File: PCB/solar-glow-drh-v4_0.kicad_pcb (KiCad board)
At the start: 2 copper layers, 50.8 x 88.9 mm, 67 parts, among them J1 UPDI hdr, SW2 LED master, U1 AVR64DD28 (VQFN28), U3 ADXL367, U5 NT3H2211, U6 TPS22918, U8 AEM10300, U9 TPS7A0233 (SOT23-5*)

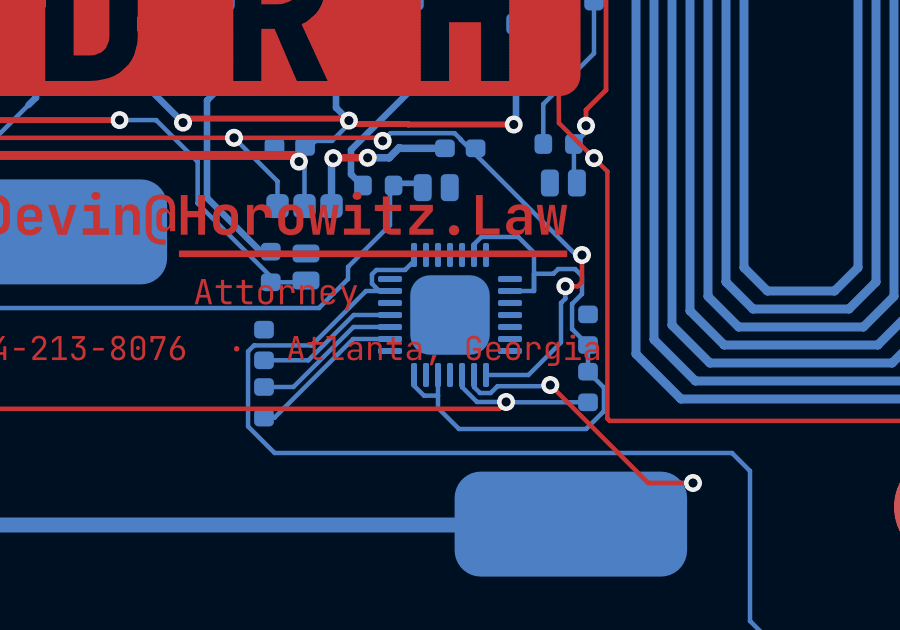
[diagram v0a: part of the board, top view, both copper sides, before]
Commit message: PCB: fix U8 AEM10300 EP land to datasheet; relabel stay-0402 parts
U8 (AEM10300, QFN-28 4x4): the reused AVR land carried a 2.65 mm exposed
pad; e-peas Fig 18 recommends a 2.30 mm thermal land. Shrink U8's EP to
2.30 mm (scoped to U8 only; U1 keeps its 2.65 mm EP). Pad centres are
unchanged so routing is intact, and the smaller EP increases pad-to-EP
clearance. Perimeter pads stay 0.20 mm wide (0.25 mm would drop the
pitch gap to 0.15 mm, below a safe margin over the 0.126 mm floor).

Relabel the three parts that stay 0402 (the package markers were
aspirational TODOs): C26 10uF, C27 10uF (100uF is not an 0402 part and
the 1F supercaps already meet the AEM STO >=100uF minimum), FB1 ferrite.
Values updated in both the board and schematic to stay consistent.

C25 (22uF) and L2 (10uH) are left as-is; they take real 0603 lands in
the follow-up KiCad pass where they can be re-placed and re-routed.

Co-Authored-By: Claude Opus 4.8 <noreply@anthropic.com>
Claude-Session: https://claude.ai/code/session_01PBK3zFENdvoGtn8yP7qPA8
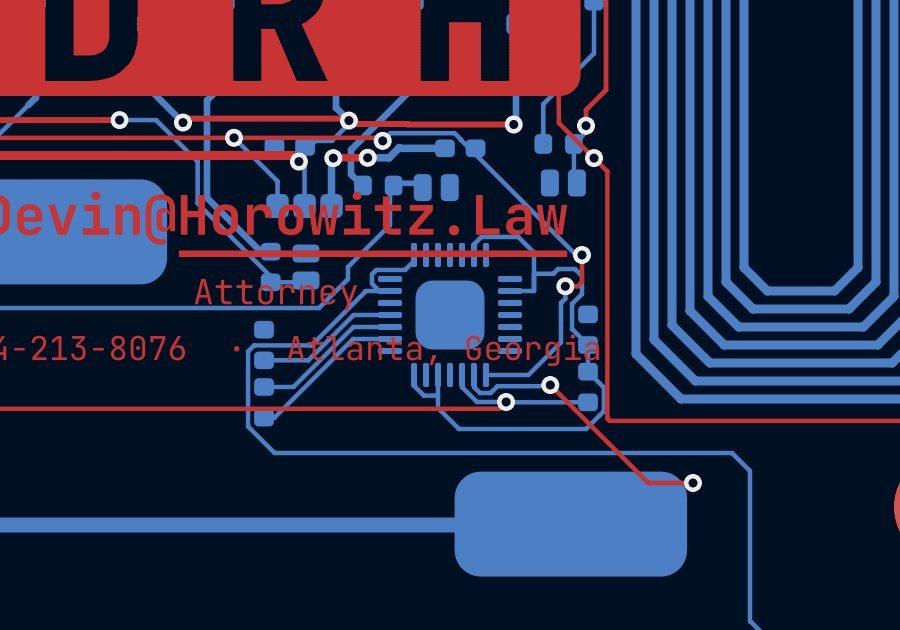
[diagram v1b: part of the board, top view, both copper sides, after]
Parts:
- C26: value 10uF *0603 -> 10uF
- C27: value 100uF *bulk -> 10uF
- FB1: value ferrite *0603 -> ferrite
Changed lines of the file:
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@@
 		(pad "EP" smd roundrect
 			(at 0 0)
-			(size 2.65 2.65)
+			(size 2.3 2.3)
 			(layers "B.Cu" "B.Mask" "B.Paste")
 			(roundrect_rratio 0.25)
@@
 			)
 		)
-		(property "Value" "10uF *0603"
+		(property "Value" "10uF"
 			(at 0 0 90)
 			(layer "F.Fab")
@@
 			)
 		)
-		(property "Value" "ferrite *0603"
+		(property "Value" "ferrite"
 			(at 0 0 90)
 			(layer "F.Fab")
@@
 			)
 		)
-		(property "Value" "100uF *bulk"
+		(property "Value" "10uF"
 			(at 0 0 90)
 			(layer "F.Fab")
